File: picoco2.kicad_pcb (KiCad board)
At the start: 2 copper layers, 53.3 x 93.2 mm, 19 parts, among them J1 Conn_01x03_Female, Q1 Q_NMOS_GDS, SW1 SW_Push, SW2 SW_Push, U1 PicoW, U2 scd30, U3 ssd1306

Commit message: update
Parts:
- removed D2: LED, LED_THT:LED_D5.0mm
- added BT1: Battery, picoco2:CR1220-2, F.Cu at (109.6, 123.7)
- added BT3: Battery, Connector_JST:JST_PH_S2B-PH-SM4-TB_1x02-1MP_P2.00mm_Horizontal, F.Cu at (99.4, 113.4)
- added C1: C, Capacitor_SMD:C_0603_1608Metric_Pad1.08x0.95mm_HandSolder, F.Cu at (113.4, 114.1)
- added C2: C, Capacitor_SMD:C_0603_1608Metric_Pad1.08x0.95mm_HandSolder, F.Cu at (113.4, 110.2)
- added C3: C, Capacitor_SMD:C_0603_1608Metric_Pad1.08x0.95mm_HandSolder, F.Cu at (106.7, 113.5)
- added D4: LED, LED_SMD:LED_0603_1608Metric_Pad1.05x0.95mm_HandSolder, F.Cu at (95.9, 122.4)
- added D5: D, Diode_SMD:D_SOD-123F, F.Cu at (142.1, 46.6)
- added J2: Micro_SD_Card, picoco2:DM3D-SF_outline, F.Cu at (127.1, 127.4)
- added J3: Conn_01x03_Female, Connector_PinSocket_2.54mm:PinSocket_1x03_P2.54mm_Vertical, F.Cu at (146.8, 115.1)
- added JP1: SolderJumper_2_Open, Jumper:SolderJumper-2_P1.3mm_Open_Pad1.0x1.5mm, F.Cu at (110.9, 55.5)
- added R10: R, Resistor_THT:R_Axial_DIN0204_L3.6mm_D1.6mm_P7.62mm_Horizontal, F.Cu at (103.1, 54.9)
- added R11: R, Resistor_THT:R_Axial_DIN0204_L3.6mm_D1.6mm_P7.62mm_Horizontal, F.Cu at (103.2, 44.9)
- added R5: R, Resistor_SMD:R_0603_1608Metric_Pad0.98x0.95mm_HandSolder, F.Cu at (103.1, 51.1)
- added R6: R, Resistor_SMD:R_0603_1608Metric_Pad0.98x0.95mm_HandSolder, F.Cu at (118.6, 116.4)
- added R7: 1K, Resistor_SMD:R_0603_1608Metric_Pad0.98x0.95mm_HandSolder, F.Cu at (99.5, 121.0)
- added R8: 10K, Resistor_SMD:R_0603_1608Metric_Pad0.98x0.95mm_HandSolder, F.Cu at (110.3, 110.3)
- added R9: R, Resistor_SMD:R_0603_1608Metric_Pad0.98x0.95mm_HandSolder, F.Cu at (103.2, 41.1)
- added U4: PCF8523T, Package_SO:SOIC-8_3.9x4.9mm_P1.27mm, F.Cu at (118.7, 111.4)
- added U5: MCP73831-2-OT, Package_TO_SOT_SMD:SOT-23-5, F.Cu at (106.9, 110.3)
- added Y1: Crystal_GND23, Crystal:Crystal_SMD_Abracon_ABS25-4Pin_8.0x3.8mm, F.Cu at (128.2, 111.7)
- BZ1: footprint Buzzer_Beeper:Buzzer_12x9.5RM7.6 -> Buzzer_Beeper:MagneticBuzzer_Kobitone_254-EMB84Q-RO
- D1: footprint Diode_THT:D_A-405_P7.62mm_Horizontal -> Diode_SMD:D_SOD-123F
- Q1: footprint Package_TO_SOT_THT:TO-220-3_Horizontal_TabDown -> Package_TO_SOT_SMD:SOT-23
- R1, R2, R3, R4: footprint Resistor_THT:R_Axial_DIN0207_L6.3mm_D2.5mm_P7.62mm_Horizontal -> Resistor_SMD:R_0603_1608Metric_Pad0.98x0.95mm_HandSolder
- U1: footprint RPi_Pico:RPi_PicoW_SMD_TH -> RPi_Pico:RPi_PicoW_SMD
- moved R3 70.7 mm to (130.3, 55.1), turned to 0 degrees
- moved Q1 62.9 mm to (135.5, 55.8), turned to 180 degrees
- moved R4 43.9 mm to (139.5, 120.8), turned to 180 degrees
- moved R2 19.4 mm to (142.8, 55.6), turned to 180 degrees
- moved D1 16.3 mm to (142.1, 40.9), turned to -90 degrees
- moved H4 10.1 mm to (97.8, 128.8)
- moved H1 10.1 mm to (145.4, 128.8)
- moved BZ1 8.33 mm to (139.4, 113.7)
- moved R1 7.26 mm to (142.8, 53.6), turned to 180 degrees
- moved BT2 1.79 mm to (145.6, 101.3)
- moved H2 1.48 mm to (97.8, 32.3)
- moved J1 1.13 mm to (146.7, 41.4)
- moved SW1 0.86 mm to (97.6, 53.4)
- moved SW2 0.85 mm to (97.6, 43.3)
- moved U1 0.68 mm to (121.7, 69.8)
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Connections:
- BT2 pad 1: Net-(BT2-Pad1) -> VBAT_AAA
- BZ1 pad 1: unconnected-(BZ1-Pad1) -> BUZZER
- BZ1 pad 2: unconnected-(BZ1-Pad2) -> GND
- D1 pad 2: Net-(D1-Pad2) -> VBAT_AAA
- J1 pad 1: Net-(D1-Pad2) -> VSYS
- J1 pad 2: Net-(BT2-Pad1) -> Net-(D1-Pad1)
- J1 pad 3: unconnected-(J1-Pad3) -> Net-(J1-Pad3)
- Q1 pad 1: unconnected-(Q1-Pad1) -> SCD30_EN
- Q1 pad 2: unconnected-(Q1-Pad2) -> SCD30_GND
- Q1 pad 3: unconnected-(Q1-Pad3) -> GND
- R1 pad 2: Net-(R1-Pad2) -> SDA
- R2 pad 2: Net-(R2-Pad2) -> SCL
- R3 pad 1: unconnected-(R3-Pad1) -> SCD30_EN
- R3 pad 2: unconnected-(R3-Pad2) -> GND
- R4 pad 1: unconnected-(R4-Pad1) -> Net-(J3-Pad2)
- R4 pad 2: unconnected-(R4-Pad2) -> GND
- SW1 pad 1: unconnected-(SW1-Pad1) -> BUT_A
- SW1 pad 2: unconnected-(SW1-Pad2) -> GND
- SW2 pad 1: unconnected-(SW2-Pad1) -> BUT_B
- SW2 pad 2: unconnected-(SW2-Pad2) -> GND
- U1 pad 1: unconnected-(U1-Pad1) -> SDA
- U1 pad 14: unconnected-(U1-Pad14) -> SCK
- U1 pad 15: unconnected-(U1-Pad15) -> MOSI
- U1 pad 16: unconnected-(U1-Pad16) -> MISO
- U1 pad 2: unconnected-(U1-Pad2) -> SCL
- U1 pad 26: Net-(R2-Pad2) -> unconnected-(U1-Pad26)
- U1 pad 27: Net-(R1-Pad2) -> unconnected-(U1-Pad27)
- U1 pad 39: Net-(D1-Pad1) -> VSYS
- U1 pad 4: unconnected-(U1-Pad4) -> SD_CS
- U1 pad 40: unconnected-(U1-Pad40) -> VBUS
- U2 pad 2: GND -> SCD30_GND
- U2 pad 3: Net-(R1-Pad2) -> SCL
- U2 pad 4: Net-(R2-Pad2) -> SCL
- U3 pad 3: Net-(R1-Pad2) -> SCL
- U3 pad 4: Net-(R2-Pad2) -> SCL
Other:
- board size 53.3 x 93.2 mm -> 54.5 x 103.4 mm

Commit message: basic layout done
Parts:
- added D2: D, Diode_THT:D_5W_P10.16mm_Horizontal, F.Cu at (48.7, 26.7)
- moved JP1 115.4 mm to (8.48, 2.34), turned to 90 degrees
- moved D1 113.9 mm to (44.1, 99.1), turned to 180 degrees
- moved D5 112.4 mm to (44.2, 101.8), turned to 180 degrees
- moved R5 108.8 mm to (3.30, 94.4)
- moved R2 108.1 mm to (41.8, 94.0)
- moved R1 108.1 mm to (41.8, 91.7)
- moved R7 99.8 mm to (4.22, 91.2)
- moved D4 99.4 mm to (1.12, 92.5)
- moved BZ1 99.3 mm to (44.3, 84.8)
- moved BT1 99.3 mm to (14.6, 94.7)
- moved U5 99.1 mm to (12.1, 81.3)
- moved R9 99.1 mm to (24.0, 100.7)
- moved J2 99.1 mm to (32.2, 98.6)
- moved R8 99.0 mm to (15.6, 81.3)
- moved Y1 99.0 mm to (33.6, 82.7)
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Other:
- outline, holes or cut-outs redrawn

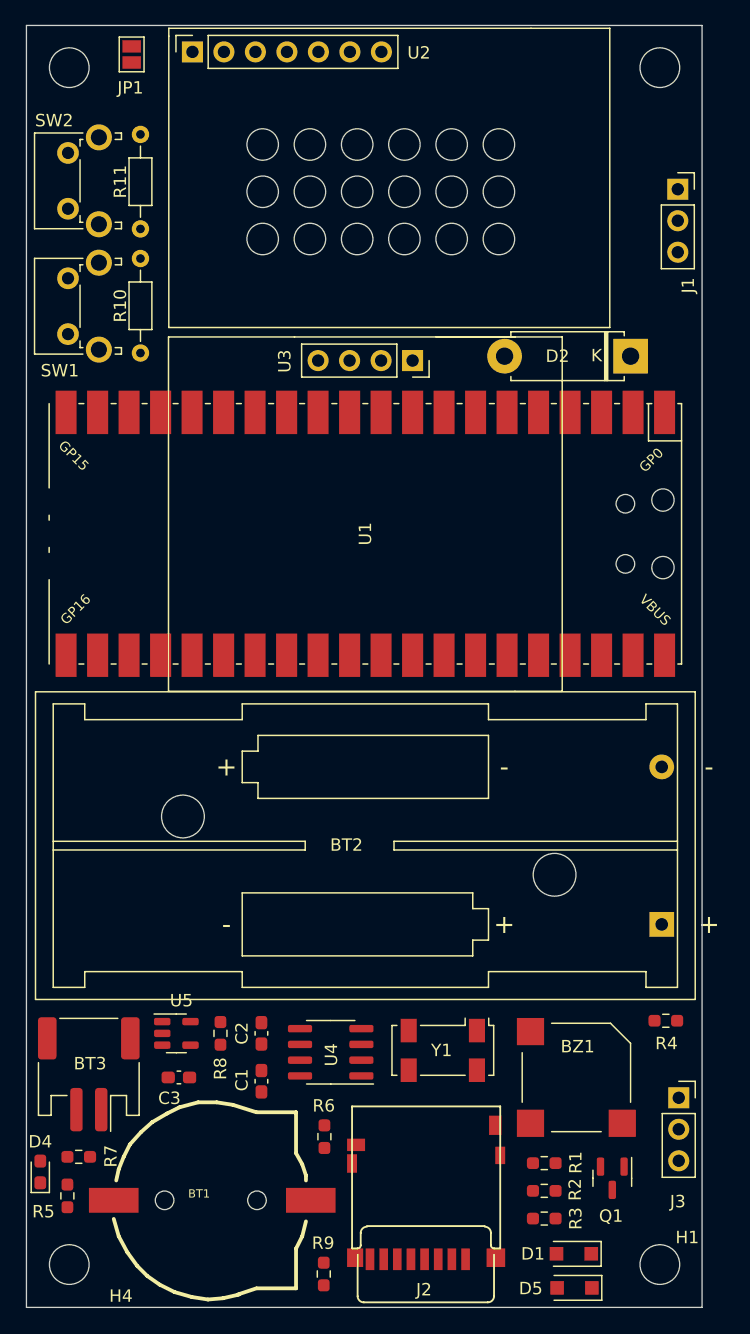
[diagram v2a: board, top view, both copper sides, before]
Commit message: rounded edges
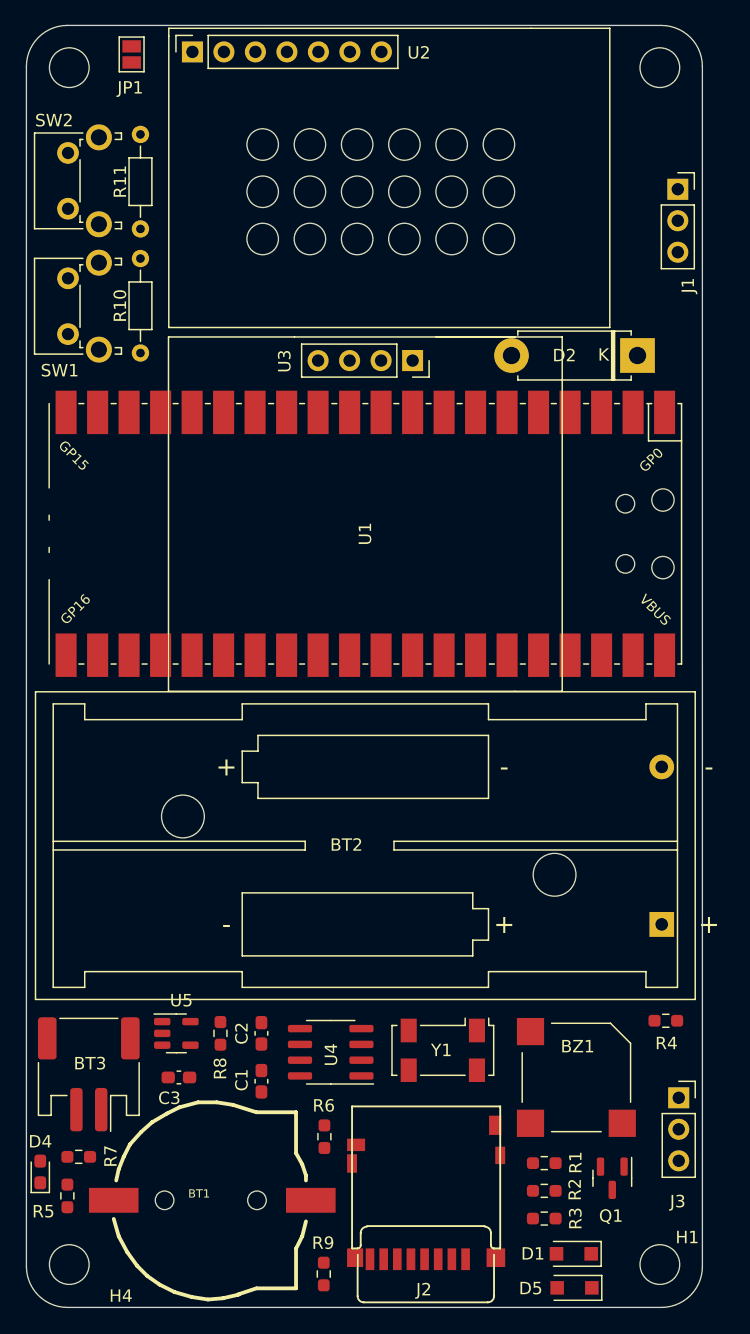
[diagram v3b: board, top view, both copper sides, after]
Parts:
- moved D2 0.56 mm to (49.3, 26.6)
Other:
- outline, holes or cut-outs redrawn
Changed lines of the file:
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@@
   )
   (footprint "Diode_THT:D_5W_P10.16mm_Horizontal" (layer "F.Cu")
-    (at 48.7172 26.67 180)
+    (at 49.276 26.6192 180)
     (descr "Diode, 5W series, Axial, Horizontal, pin pitch=10.16mm, , length*diameter=8.9*3.7mm^2, , http://www.diodes.com/_files/packages/8686949.gif")
     (tags "Diode 5W series Axial Horizontal pin pitch 10.16mm  length 8.9mm diameter 3.7mm")
@@
   (gr_circle (center 26.67 17.2212) (end 26.67 18.4912) (layer "Edge.Cuts") (width 0.1) (fill none))
   (gr_circle (center 22.86 13.4112) (end 22.86 14.6812) (layer "Edge.Cuts") (width 0.1) (fill none))
-  (gr_rect (start 54.483 103.378) (end 0 0) (layer "Edge.Cuts") (width 0.1) (fill none))
+  (gr_arc (start 51.2064 0) (mid 53.541267 0.967133) (end 54.5084 3.302) (layer "Edge.Cuts") (width 0.1))
   (gr_circle (center 30.48 9.6012) (end 30.48 10.8712) (layer "Edge.Cuts") (width 0.1) (fill none))
+  (gr_line (start 51.2064 0) (end 3.300067 -0.001933) (layer "Edge.Cuts") (width 0.1))
   (gr_circle (center 34.29 17.2212) (end 34.29 18.4912) (layer "Edge.Cuts") (width 0.1) (fill none))
   (gr_circle (center 34.29 13.4112) (end 34.29 14.6812) (layer "Edge.Cuts") (width 0.1) (fill none))
   (gr_circle (center 38.1 17.2212) (end 38.1 18.4912) (layer "Edge.Cuts") (width 0.1) (fill none))
+  (gr_line (start -0.001933 3.300067) (end -0.001933 100.077933) (layer "Edge.Cuts") (width 0.1))
   (gr_circle (center 19.05 17.2212) (end 19.05 18.4912) (layer "Edge.Cuts") (width 0.1) (fill none))
   (gr_circle (center 26.67 13.4112) (end 26.67 14.6812) (layer "Edge.Cuts") (width 0.1) (fill none))
   (gr_circle (center 22.86 17.2212) (end 22.86 18.4912) (layer "Edge.Cuts") (width 0.1) (fill none))
+  (gr_line (start 3.300067 103.379933) (end 51.208333 103.379933) (layer "Edge.Cuts") (width 0.1))
   (gr_circle (center 30.48 13.4112) (end 30.48 14.6812) (layer "Edge.Cuts") (width 0.1) (fill none))
   (gr_circle (center 19.05 9.6012) (end 19.05 10.8712) (layer "Edge.Cuts") (width 0.1) (fill none))
   (gr_circle (center 30.48 17.2212) (end 30.48 18.4912) (layer "Edge.Cuts") (width 0.1) (fill none))
   (gr_circle (center 26.67 9.6012) (end 26.67 10.8712) (layer "Edge.Cuts") (width 0.1) (fill none))
+  (gr_arc (start 54.510333 100.077933) (mid 53.5432 102.4128) (end 51.208333 103.379933) (layer "Edge.Cuts") (width 0.1))
+  (gr_arc (start 3.300067 103.379933) (mid 0.9652 102.4128) (end -0.001933 100.077933) (layer "Edge.Cuts") (width 0.1))
+  (gr_arc (start -0.001933 3.300067) (mid 0.9652 0.9652) (end 3.300067 -0.001933) (layer "Edge.Cuts") (width 0.1))
+  (gr_line (start 54.510333 100.077933) (end 54.5084 3.302) (layer "Edge.Cuts") (width 0.1))
   (gr_circle (center 38.1 13.4112) (end 38.1 14.6812) (layer "Edge.Cuts") (width 0.1) (fill none))
   (gr_circle (center 19.05 13.4112) (end 19.05 14.6812) (layer "Edge.Cuts") (width 0.1) (fill none))

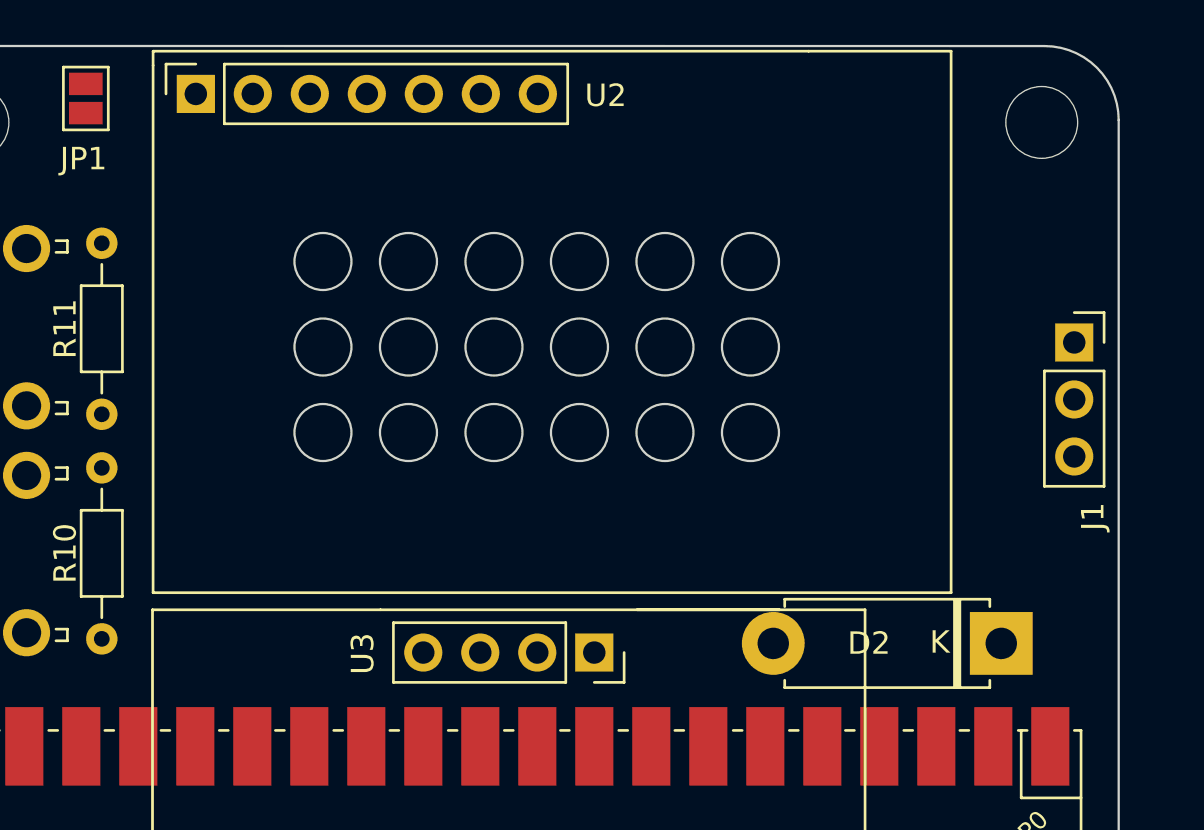
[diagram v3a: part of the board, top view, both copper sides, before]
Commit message: added i2c resistors
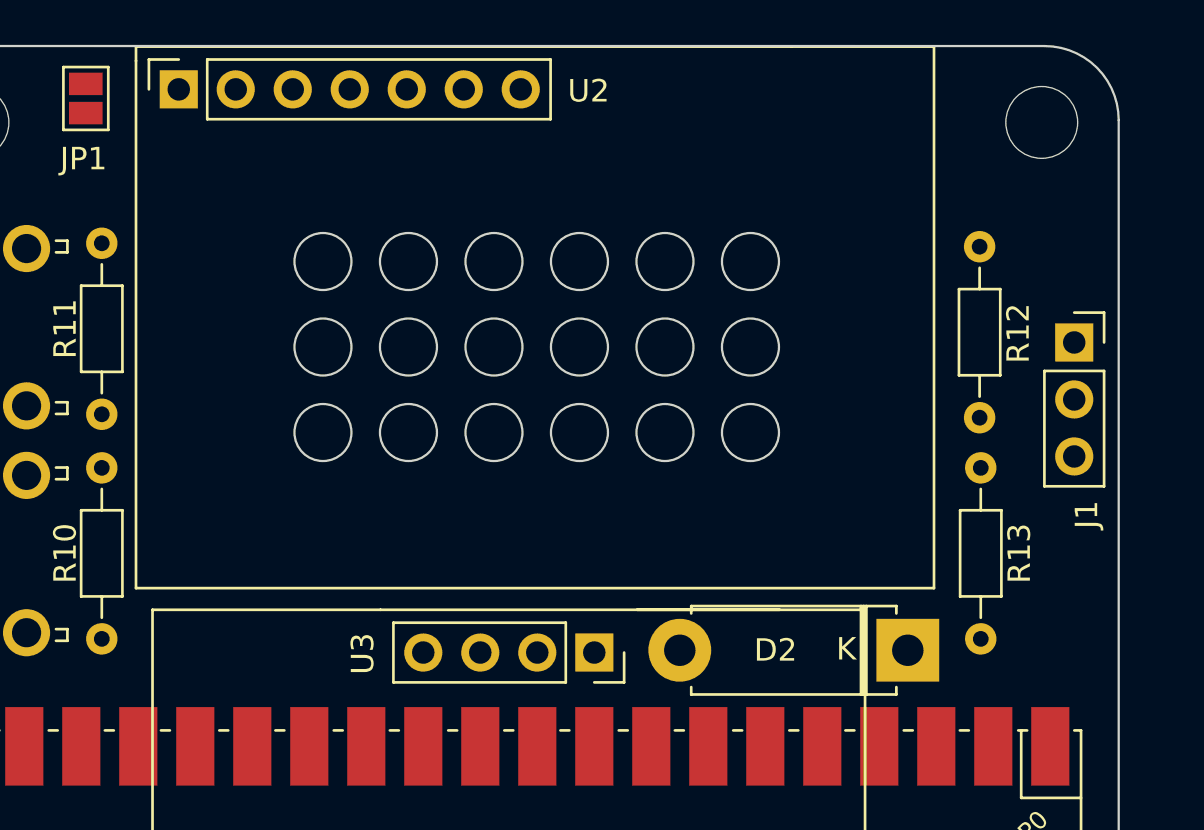
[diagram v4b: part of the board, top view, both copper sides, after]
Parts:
- added R12: R, Resistor_THT:R_Axial_DIN0204_L3.6mm_D1.6mm_P7.62mm_Horizontal, F.Cu at (48.3, 16.6)
- added R13: R, Resistor_THT:R_Axial_DIN0204_L3.6mm_D1.6mm_P7.62mm_Horizontal, F.Cu at (48.4, 26.4)
- moved D2 4.18 mm to (45.1, 26.9)
- moved U2 0.79 mm to (12.6, 1.93)
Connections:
- U1 pad 10: unconnected-(U1-Pad10) -> BUZZER
- U1 pad 11: unconnected-(U1-Pad11) -> RTC_INT
- U1 pad 5: unconnected-(U1-Pad5) -> BUT_A
- U1 pad 6: unconnected-(U1-Pad6) -> BUT_B
- U1 pad 7: unconnected-(U1-Pad7) -> SCD30_EN
- U1 pad 9: unconnected-(U1-Pad9) -> WRITE_EN

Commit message: update
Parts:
- moved R13 7.58 mm to (48.8, 18.8), turned to -90 degrees
- moved D5 1.99 mm to (42.2, 101.7)
- moved D1 1.94 mm to (42.2, 98.9)
- moved R4 0.67 mm to (52.2, 80.4)
- moved D2 0.59 mm to (45.7, 26.7)
- moved J1 0.55 mm to (52.5, 12.7)
- moved R12 0.51 mm to (48.8, 16.5)
- moved C3 0.51 mm to (12.0, 85.2)
- moved JP1 0.48 mm to (8.64, 2.79)
- moved Q1 0.46 mm to (47.7, 93.0)
- moved Y1 0.43 mm to (34.0, 82.8)
- moved R7 0.42 mm to (4.32, 90.8)
- moved C1 0.42 mm to (19.4, 85.0)
- moved C2 0.42 mm to (19.4, 81.2)
- moved U4 0.42 mm to (24.9, 82.7)
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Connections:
- U2 pad 4: SCL -> SDA
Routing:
- net Net-(D5-Pad1): track 0.00 -> 90.2 mm, vias 0 -> 1
- net VBAT_AAA: track 0.00 -> 60.8 mm, vias 0 -> 2
- net +3V3: track 0.00 -> 59.1 mm, vias 0 -> 6
- net GND: track 0.00 -> 59.0 mm, vias 0 -> 6
- net VSYS: track 0.00 -> 38.7 mm, vias 0 -> 1
- net SDA: track 0.00 -> 29.2 mm, vias 0 -> 3
- net Net-(D1-Pad1): track 0.00 -> 18.4 mm, vias 0 -> 1
- net SCD30_GND: track 0.00 -> 14.7 mm, vias 0 -> 3
